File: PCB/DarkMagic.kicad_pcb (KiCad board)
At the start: 6 copper layers, 157 x 73 mm, 212 parts, among them IC1 5PB1106PGGI8, IC10 MMBT3904-AQ, IC11 MMBT3904-AQ, IC12 SN74LVC1G125DBVT, IC13 SN74LVC1G125DBVT, IC14 LM3940IMP-3.3_NOPB, IC15 SN74LVC1G125DBVT, IC17 LM393DR, IC2 ESP32-WROOM-32UE-N16, IC3 MMBT3904-AQ, IC4 MMBT3904-AQ, IC5 W5500, IC6 CP2102N-A02-GQFN24, IC7 USBLC6-2SC6, IC8 LMR33640ADDAR, J1 USB_C_Receptacle_USB2.0_16P, J2 TMJ0026ABNL, J3 5747842-2, J4 Screw_Terminal_01x02, J5 Screw_Terminal_01x02, J6 5747842-2, J7 171825-2, J9 Conn_01x04, Q1 SQ2319ADS-T1_BE3, Q2 SQ2348ES-T1_BE3, U1 SC16IS752IPW_128, U2 SC16IS752IPW_128, U3 CD74HC138QM96Q1, U4 SC16IS752IPW_128, U5 SC16IS752IPW_128, U6 SC16IS752IPW_128, U7 SC16IS752IPW_128, Y2 ASE-14.7456MHZ-LC-T, Y3 ASE-25.000MHZ-LC-T

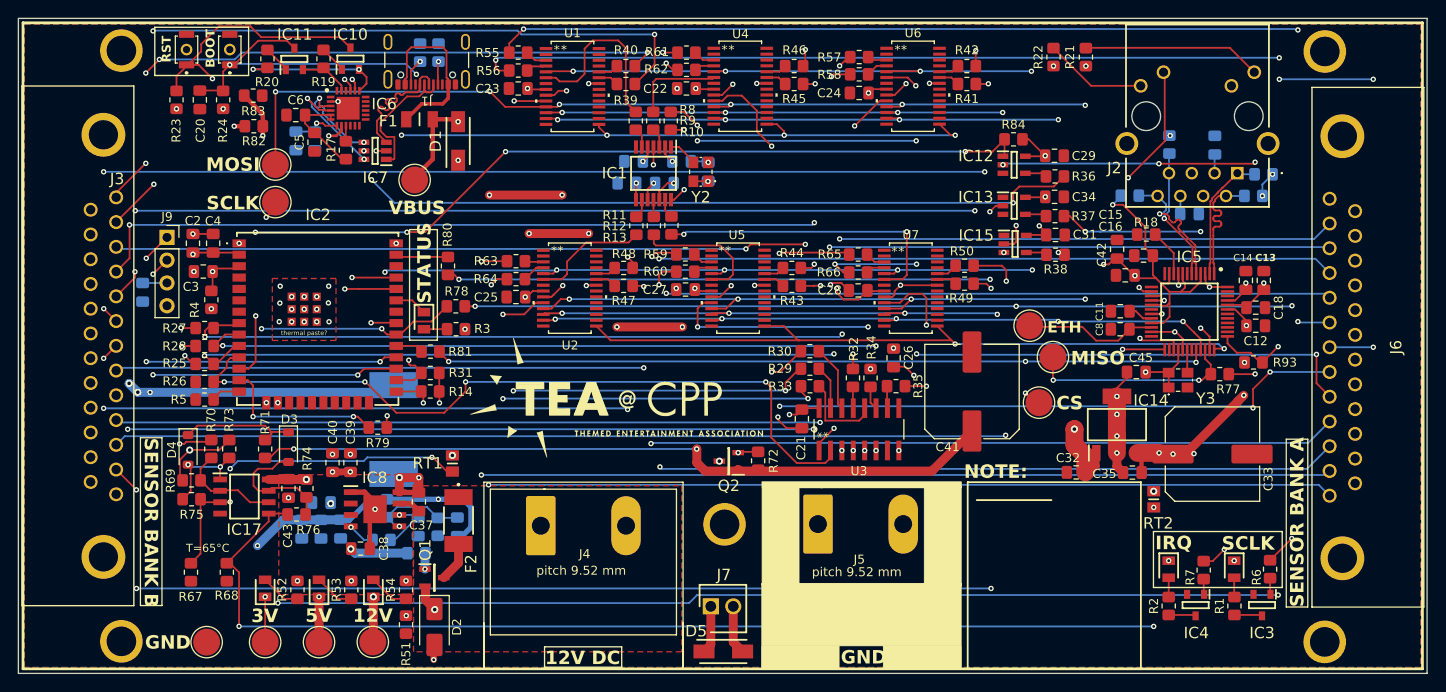
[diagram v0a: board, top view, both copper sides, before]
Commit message: Updated PDF schematic, tweaked connections
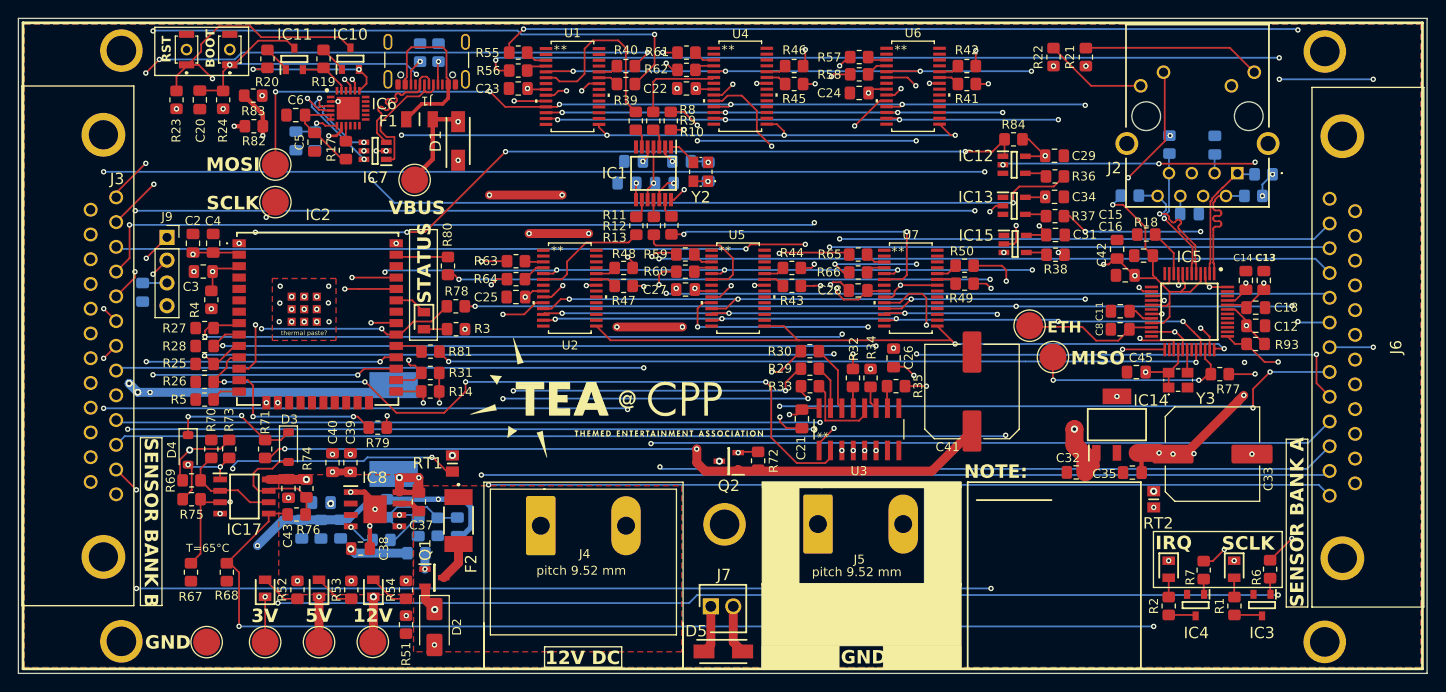
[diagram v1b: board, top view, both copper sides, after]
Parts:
- removed TP10: TestPoint, TestPoint:TestPoint_Pad_D3.0mm
- moved R93 2.07 mm to (213.7, 58.2), turned to 180 degrees
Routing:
- net GND: track 85.7 -> 64.1 mm, vias 69 -> 65
- net /ESP_SCSN: track 91.7 -> 86.2 mm, vias 4 -> 2
- net +3V3: track 216.1 -> 219.0 mm
- net Net-(D3-K): track 12.6 -> 14.8 mm, vias 0 -> 2
- net /W5500_RST: track 169.4 -> 167.2 mm
- removed copper zone on In3.Cu, net /12VIN
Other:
- board text added: "0.1uF"
- board text removed: "CS"
